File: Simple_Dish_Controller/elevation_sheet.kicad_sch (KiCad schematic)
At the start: 19 parts, among them J4 Conn_01x03_Pin, J5 Elevation DE-15, Q1 MMBT2222A, Q2 MMBT2222A, U2 74LS32, U3 74LS08, U4 NE555D

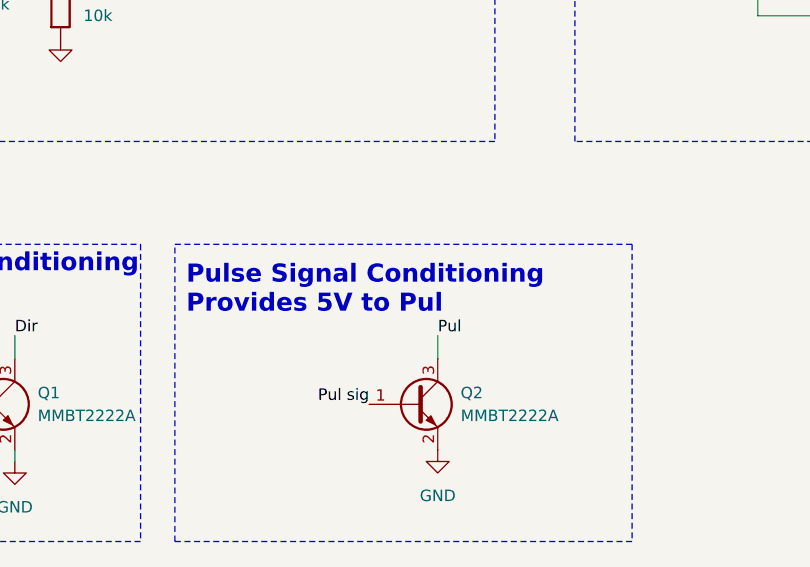
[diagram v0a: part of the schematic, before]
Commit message: PCB outline defined, origin and drill holes established, hole positioning completed. Beginning component placement.
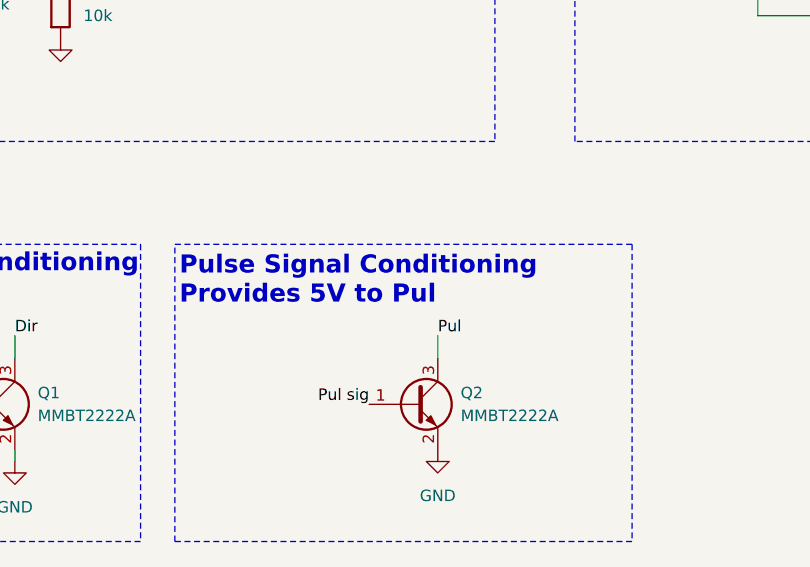
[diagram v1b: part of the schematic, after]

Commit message: Final version of the PCB.Production files were generated in -Production- folder
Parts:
- C5: value 0.1uF -> 100nF; LCSC Part (none) -> C24497
- C6: LCSC Part (none) -> C24497
- C7: LCSC Part (none) -> C13585
- Q1, Q2: LCSC Part (none) -> C8512
- R10: LCSC Part (none) -> C4410
- R2: LCSC Part (none) -> C17984
- R3, R4, R6, R7, R8, R9: LCSC Part (none) -> C17902
- R5: LCSC Part (none) -> C2907522
- U2: LCSC Part (none) -> C116812
- U3: LCSC Part (none) -> C6802
- U4: LCSC Part (none) -> C234230
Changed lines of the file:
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@@
 			)
 		)
-		(property "LCSC Part" ""
+		(property "LCSC Part" "C17902"
 			(at 96.52 76.2 0)
 			(effects
@@
 					(size 1.27 1.27)
 				)
+				(hide yes)
 			)
 		)
@@
 			)
 		)
-		(property "LCSC Part" ""
+		(property "LCSC Part" "C17902"
 			(at 63.5 86.36 0)
 			(effects
@@
 					(size 1.27 1.27)
 				)
+				(hide yes)
 			)
 		)
@@
 			)
 		)
-		(property "LCSC Part" ""
+		(property "LCSC Part" "C116812"
 			(at 111.76 68.58 0)
 			(effects
@@
 					(size 1.27 1.27)
 				)
+				(hide yes)
 			)
 		)
@@
 			)
 		)
-		(property "LCSC Part" ""
+		(property "LCSC Part" "C24497"
 			(at 152.4 82.55 0)
 			(effects
@@
 					(size 1.27 1.27)
 				)
+				(hide yes)
 			)
 		)
@@
 			)
 		)
-		(property "LCSC Part" ""
+		(property "LCSC Part" "C17984"
 			(at 193.04 53.34 0)
 			(effects
@@
 					(size 1.27 1.27)
 				)
+				(hide yes)
 			)
 		)
@@
 			)
 		)
-		(property "LCSC Part" ""
+		(property "LCSC Part" "C17902"
 			(at 101.6 76.2 0)
 			(effects
@@
 					(size 1.27 1.27)
 				)
+				(hide yes)
 			)
 		)
@@
 			)
 		)
-		(property "LCSC Part" ""
+		(property "LCSC Part" "C8512"
 			(at 114.3 132.08 0)
 			(effects
@@
 					(size 1.27 1.27)
 				)
+				(hide yes)
 			)
 		)
@@
 			)
 		)
-		(property "LCSC Part" ""
+		(property "LCSC Part" "C2907522"
 			(at 193.04 71.12 0)
 			(effects
@@
 					(size 1.27 1.27)
 				)
+				(hide yes)
 			)
 		)
@@
 			)
 		)
-		(property "LCSC Part" ""
+		(property "LCSC Part" "C4410"
 			(at 53.34 132.08 0)
 			(effects
@@
 					(size 1.27 1.27)
 				)
+				(hide yes)
 			)
 		)
@@
 			)
 		)
-		(property "LCSC Part" ""
+		(property "LCSC Part" "C6802"
 			(at 83.82 80.01 0)
 			(effects
@@
 					(size 1.27 1.27)
 				)
+				(hide yes)
 			)
 		)
@@
 			)
 		)
-		(property "LCSC Part" ""
+		(property "LCSC Part" "C13585"
 			(at 161.29 82.55 0)
 			(effects
@@
 					(size 1.27 1.27)
 				)
+				(hide yes)
 			)
 		)
@@
 			)
 		)
-		(property "LCSC Part" ""
+		(property "LCSC Part" "C6802"
 			(at 83.82 55.88 0)
 			(effects
@@
 					(size 1.27 1.27)
 				)
+				(hide yes)
 			)
 		)
@@
 			)
 		)
-		(property "LCSC Part" ""
+		(property "LCSC Part" "C17902"
 			(at 74.93 87.63 0)
 			(effects
@@
 					(size 1.27 1.27)
 				)
+				(hide yes)
 			)
 		)
@@
 			)
 		)
-		(property "LCSC Part" ""
+		(property "LCSC Part" "C17902"
 			(at 74.93 63.5 0)
 			(effects
@@
 					(size 1.27 1.27)
 				)
+				(hide yes)
 			)
 		)
@@
 			)
 		)
-		(property "Value" "0.1uF"
+		(property "Value" "100nF"
 			(at 163.83 52.0699 0)
 			(effects
@@
 			)
 		)
-		(property "LCSC Part" ""
+		(property "LCSC Part" "C24497"
 			(at 160.02 50.8 0)
 			(effects
@@
 					(size 1.27 1.27)
 				)
+				(hide yes)
 			)
 		)
@@
 			)
 		)
-		(property "LCSC Part" ""
+		(property "LCSC Part" "C17902"
 			(at 63.5 62.23 0)
 			(effects
@@
 					(size 1.27 1.27)
 				)
+				(hide yes)
 			)
 		)
@@
 			)
 		)
-		(property "LCSC Part" ""
+		(property "LCSC Part" "C234230"
 			(at 176.53 64.77 0)
 			(effects
@@
 					(size 1.27 1.27)
 				)
+				(hide yes)
 			)
 		)
@@
 			)
 		)
-		(property "LCSC Part" ""
+		(property "LCSC Part" "C8512"
 			(at 67.31 132.08 0)
 			(effects
@@
 					(size 1.27 1.27)
 				)
+				(hide yes)
 			)
 		)
